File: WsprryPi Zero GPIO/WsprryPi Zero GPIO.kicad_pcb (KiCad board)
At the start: 2 copper layers, 65 x 30 mm, 28 parts, among them J1 SMA_Adafruit_1865, J12 Conn_01x03, J41 J81/J82 LPF sockets, SW11 SKRPANE010, T22 YA9308-AEC, T40 YA9308-AEC, U10 Raspberry Pi 40-pin HAT inter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, U32 LTC6432AIUF-15#PBF, U50 TPS22918DBVR

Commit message: Remove outdated designs
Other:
- board text added: "Wsprry Pi Universal v1.0.0 GPIO-Based WSPR Copyright © 2026 Lee C. Bussy [AA0NT]"

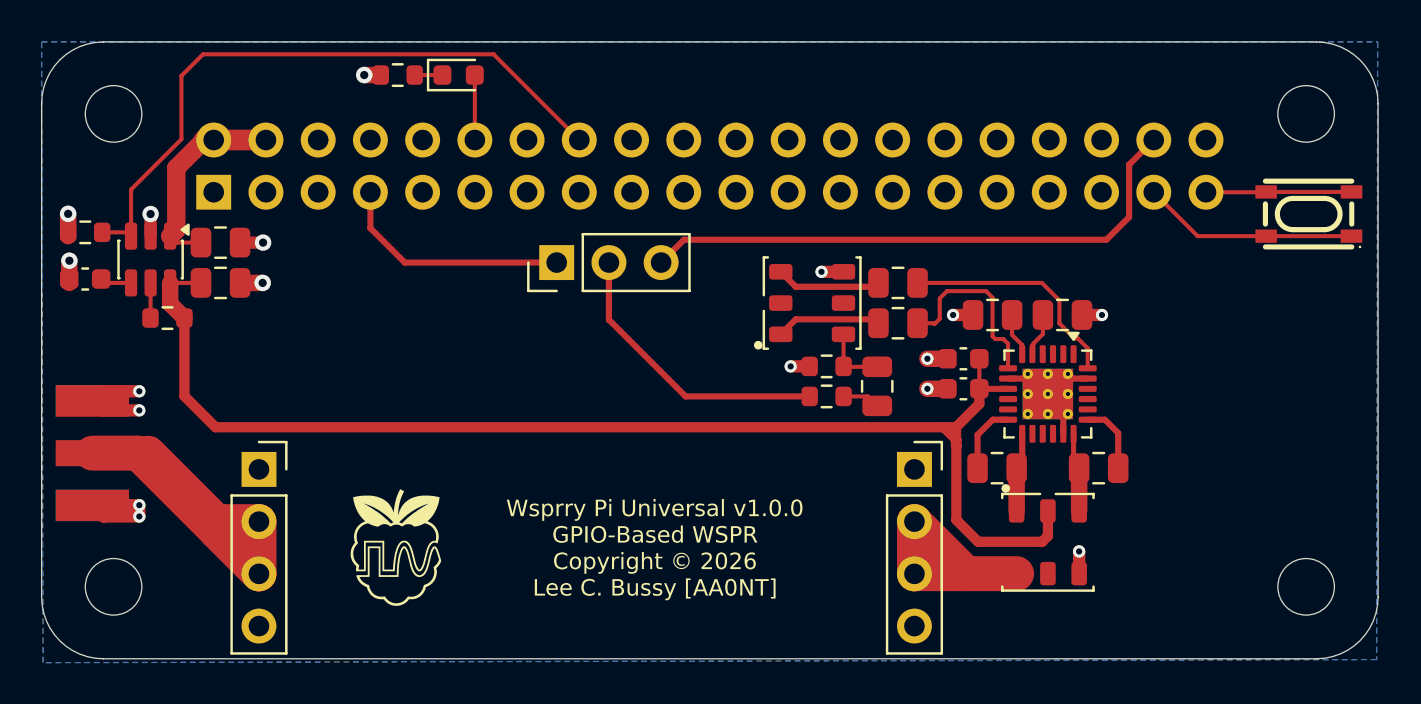
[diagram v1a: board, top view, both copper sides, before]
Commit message: Update cap type
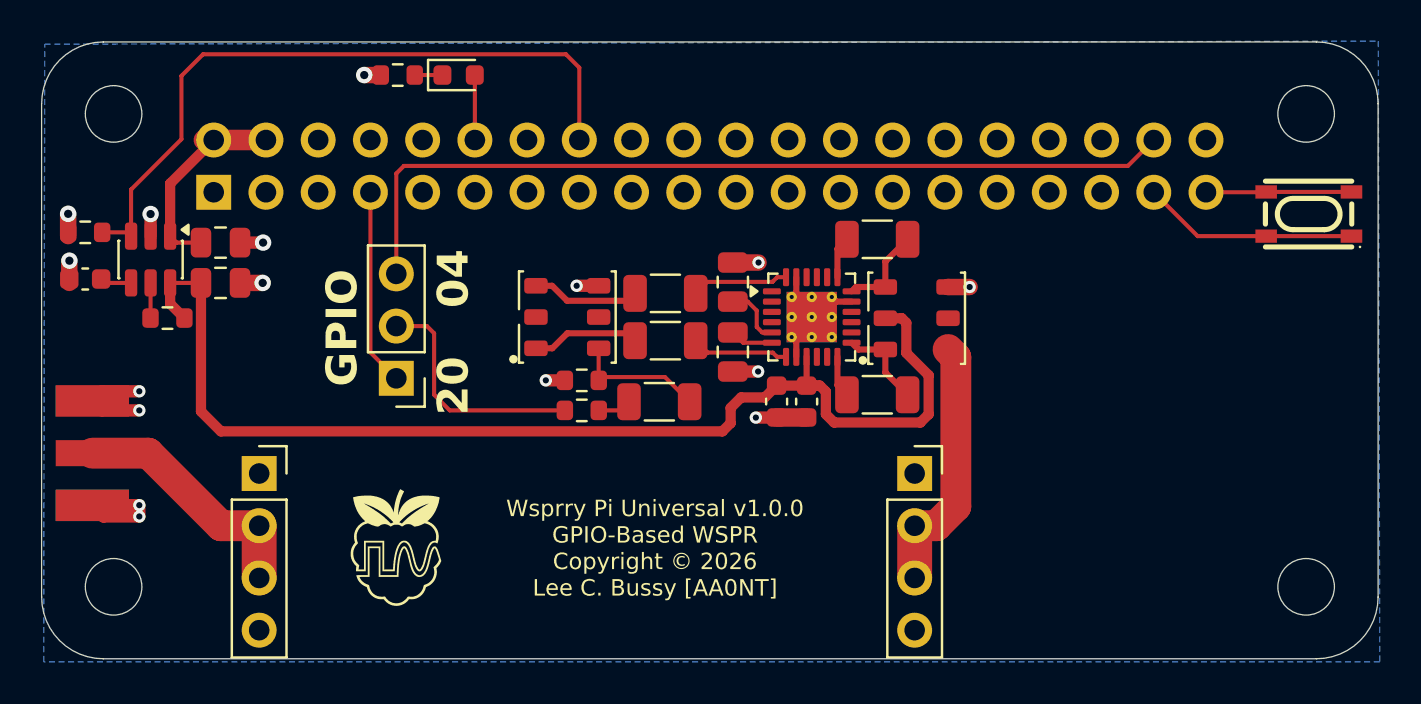
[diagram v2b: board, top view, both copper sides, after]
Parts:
- removed C30: 1µF, wsprrypi-zero-gpio:C_0805_2012Metric
- removed the C36 at (146.5, 90.7)
- added C34: 1µF, wsprrypi-zero-gpio:C_0805_2012Metric, F.Cu at (133.6, 85.1)
- added C38: 1µF, wsprrypi-zero-gpio:C_1206_3216Metric, F.Cu at (140.6, 79.6)
- C21, C31, C32, C37: footprint wsprrypi-zero-gpio:C_0805_2012Metric -> wsprrypi-zero-gpio:C_1206_3216Metric
- moved C32 19.3 mm to (130.3, 82.2), turned to 0 degrees
- moved C33 12.7 mm to (133.6, 81.7), turned to -90 degrees
- moved T41 12.6 mm to (142.6, 83.4), turned to 90 degrees
- moved U31 12.1 mm to (137.5, 83.4), turned to 0 degrees
- moved R21 11.9 mm to (126.3, 87.9)
- moved R22 11.9 mm to (126.3, 86.5)
- moved T21 11.9 mm to (125.6, 83.4)
- moved C31 11.7 mm to (130.3, 84.5)
- moved C37 11.3 mm to (140.6, 87.2), turned to 0 degrees
- moved C21 10.6 mm to (130.0, 87.5), turned to 0 degrees
- moved J12 9.62 mm to (117.2, 86.4), turned to 180 degrees
- moved C36 9.10 mm to (135.7, 87.5), turned to 90 degrees
- moved C35 7.90 mm to (137.2, 87.5), turned to 90 degrees
- moved J42 0.20 mm to (126.5, 91.0)
- renumbered C34 to C35, C35 to C36, C53 to C52, C55 to C53, J1 to J41, J41 to J42, R20 to R21, R21 to R22, R52 to R51, R54 to R52, T22 to T21, T40 to T41, U10 to U11, U32 to U31, U50 to U51
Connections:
- C31 pad 1: /RF_DIFF_P -> /RF_DIFF_N
- C31 pad 2: Net-(U32-+IN) -> Net-(U31--IN)
- C32 pad 1: GND -> /RF_DIFF_P
- C32 pad 2: Net-(U32-NFILT2) -> Net-(U31-+IN)
- C33 pad 2: Net-(U32-NFILT1) -> Net-(U31-NFILT2)
- C37 pad 1: Net-(U32-+FDBK) -> Net-(U31--FDBK)
- C37 pad 2: /AMP_OUT_P -> /AMP_OUT_N
- U31 pad 12: Net-(U32--FDBK) -> Net-(U31--FDBK)
- U31 pad 19: Net-(U32-+FDBK) -> Net-(U31-+FDBK)
- U31 pad 24: Net-(U32-+IN) -> Net-(U31-+IN)
- U31 pad 5: Net-(U32-NFILT2) -> Net-(U31-NFILT2)
- U31 pad 6: Net-(U32-NFILT1) -> Net-(U31-NFILT1)
- U31 pad 7: Net-(U32--IN) -> Net-(U31--IN)
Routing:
- net /GPIO20: track 27.9 -> 42.4 mm
- net /FINAL_OUT: track 26.0 -> 12.1 mm
- net Net-(U32-+IN): track 11.2 -> 0.00 mm
- net Net-(U32--IN): track 9.01 -> 0.00 mm
- net /SW_5V: track 62.6 -> 55.9 mm
- net Net-(U31-+IN): track 0.00 -> 4.72 mm
- net Net-(U31--IN): track 0.00 -> 4.72 mm
- net Net-(U32-+FDBK): track 3.46 -> 0.00 mm
- net Net-(U32--FDBK): track 3.41 -> 0.00 mm
- net Net-(T21-PRI1): track 3.21 -> 6.57 mm
- net Net-(U31-NFILT2): track 0.00 -> 2.99 mm
- net /GPIO_RF: track 14.1 -> 11.6 mm
- net Net-(U32-NFILT2): track 2.12 -> 0.00 mm
- net Net-(U32-NFILT1): track 2.11 -> 0.00 mm
- net Net-(U31-NFILT1): track 0.00 -> 2.11 mm
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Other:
- board text added: "04"
- board text added: "20"
- board text added: "GPIO"

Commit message: Swap transformer
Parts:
- T21, T41: value YA9308-AEC -> WBC2-1TLC; footprint wsprrypi-zero-gpio:Coilcraft_YA9308 -> wsprrypi-zero-gpio:Coilcraft_WBC2-1TLC
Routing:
- net GND: track 34.8 -> 38.9 mm, vias 16 -> 345
- net /GPIO_RF: track 11.6 -> 9.89 mm
- net /TX_OUT: track 12.7 -> 13.9 mm
- added copper zone on F.Cu, net GND
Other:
- board text added: "Wsprry Pi Universal v1.0.0 GPIO-Based WSPR (160m-6m) Copyright © 2026 Lee C. Bussy [AA0NT]"
- board text removed: "Wsprry Pi Universal v1.0.0 GPIO-Based WSPR Copyright © 2026 Lee C. Bussy [AA0NT]"
